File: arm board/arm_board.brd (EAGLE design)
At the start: 76.2 x 159.1 mm, 125 parts, among them J1 APPPP45_PCB_HORIZ_RIGHT, J17 APPPP45_PCB_HORIZ_RIGHT, J18 APPPP45_PCB_HORIZ_RIGHT, J19 ENCODER, J2 APPPP45_PCB_HORIZ_RIGHT, J20 ENCODER, J21 ENCODER, J22 ENCODER, J24 ENCODER, J3 APPPP45_PCB_HORIZ_RIGHT, J5 SERVOMOLEX_SL_VERT_TH, J6 SL02, Q1 Q_IRF7437SMD, U1 TIVA-1294

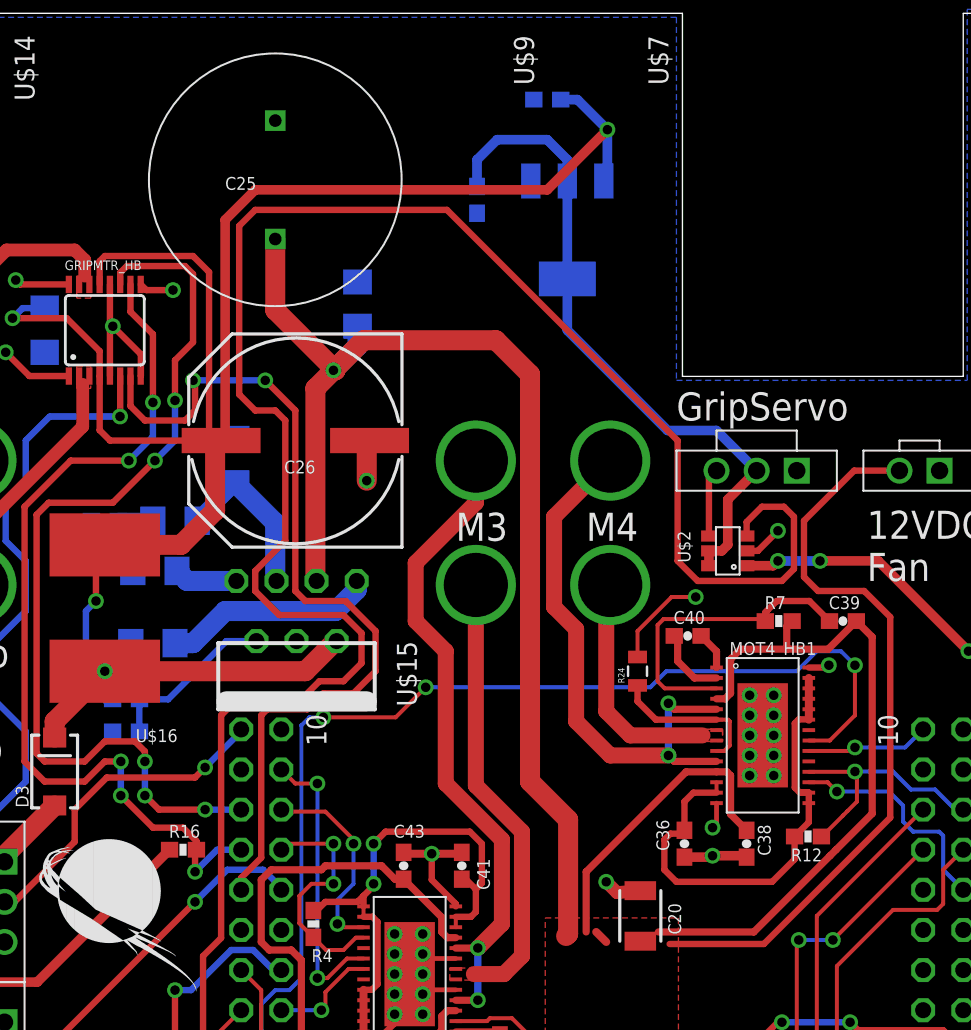
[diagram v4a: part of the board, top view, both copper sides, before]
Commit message: Swapped servo regulator input to draw from 12V line
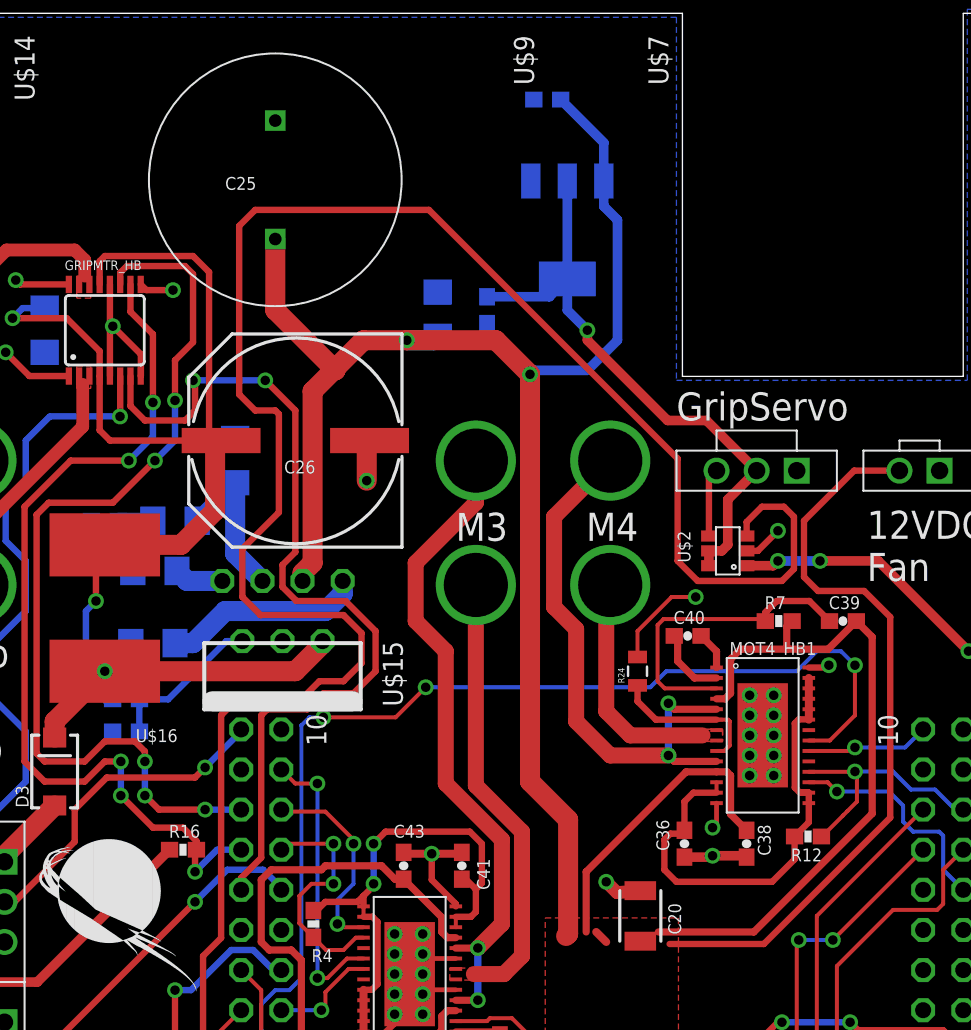
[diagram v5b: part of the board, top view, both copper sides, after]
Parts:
- moved C13 7.01 mm to (36.2, 140.3)
- moved C32 5.12 mm to (33.1, 140.1)
- moved U$15 0.89 mm to (23.2, 119.4)
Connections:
- net 12VMTR_PWR: now also C12.1, U$18.3
- net 7VMTR_PWR: no longer C12.1, U$18.3
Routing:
- net 7VMTR_PWR: track 114.7 -> 67.1 mm, vias 3 -> 2
- net 12VMTR_PWR: track 409.5 -> 431.8 mm, vias 5 -> 6
- net 5VSERVO_PWR: track 42.7 -> 38.0 mm, vias 0 -> 1
- net GRIPMTR_PHASE: track 55.9 -> 56.9 mm
- net N$9: track 4.02 -> 3.13 mm
- net N$10: track 11.0 -> 10.1 mm
- net N$33: track 25.5 -> 24.7 mm
- net N$15: track 13.5 -> 12.7 mm

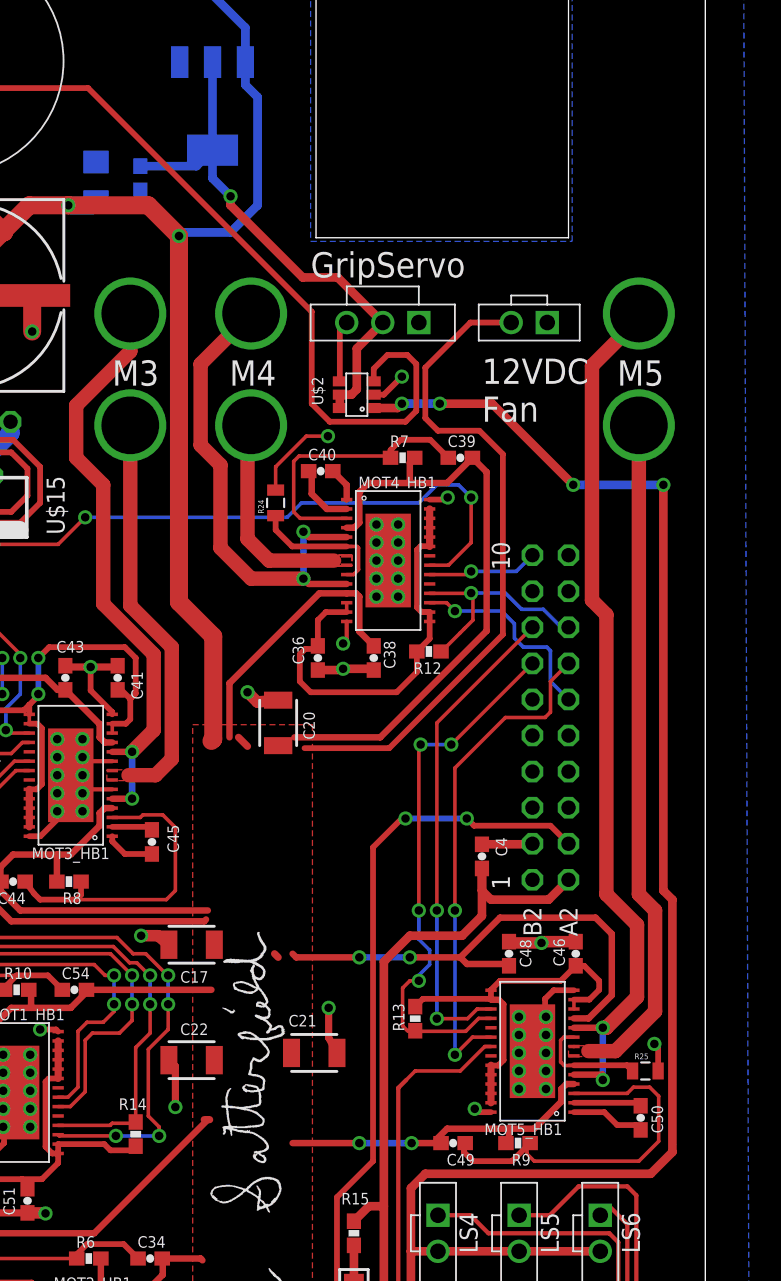
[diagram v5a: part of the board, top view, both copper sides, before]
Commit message: Changed sense resistor size
Miscalculated originally; it needs 2 watt rating
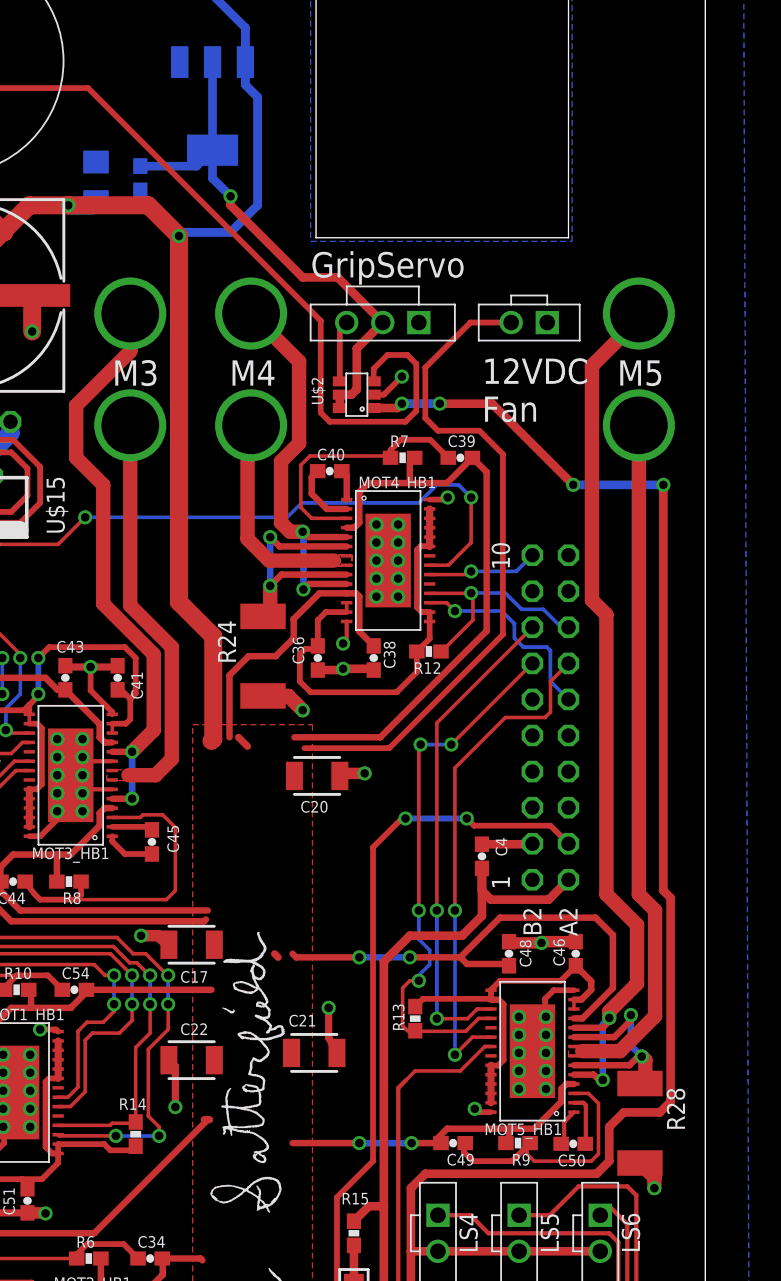
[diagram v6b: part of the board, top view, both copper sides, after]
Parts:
- removed R25: .22, SparkFun-Resistors:0805
- added R28: .22, SparkFun-Resistors:R2512
- R24: device SparkFun-Resistors:0805 -> SparkFun-Resistors:R2512
- moved R24 10.8 mm to (44.8, 106.7), turned to 270 degrees
- moved C50 5.09 mm to (66.7, 72.3), turned to 180 degrees
- moved C20 4.63 mm to (48.6, 98.2), turned to 180 degrees
- moved C40 0.63 mm to (49.5, 119.7)
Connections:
- net GND: now also R28.2; no longer R25.2
- net N$6: now also R28.1; no longer R25.1
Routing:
- net N$26: track 26.6 -> 18.0 mm
- net N$6: track 7.91 -> 16.1 mm, vias 0 -> 2
- net N$5: track 9.88 -> 17.2 mm, vias 0 -> 2
- net MOT4_1: track 35.0 -> 29.0 mm
- net GND: track 178.0 -> 174.5 mm
- net N$27: track 5.22 -> 2.60 mm
- net N$20: track 20.0 -> 18.7 mm
- net N$28: track 4.79 -> 3.64 mm
- net HB_3.3_OUTPUT8: track 27.5 -> 26.4 mm
- net 12VMTR_PWR: track 431.8 -> 432.7 mm
- net LOG_PWR_3.3V: track 405.4 -> 404.5 mm
- net MOT5_2: track 47.6 -> 48.2 mm
- net MOT5_1: track 62.3 -> 62.8 mm

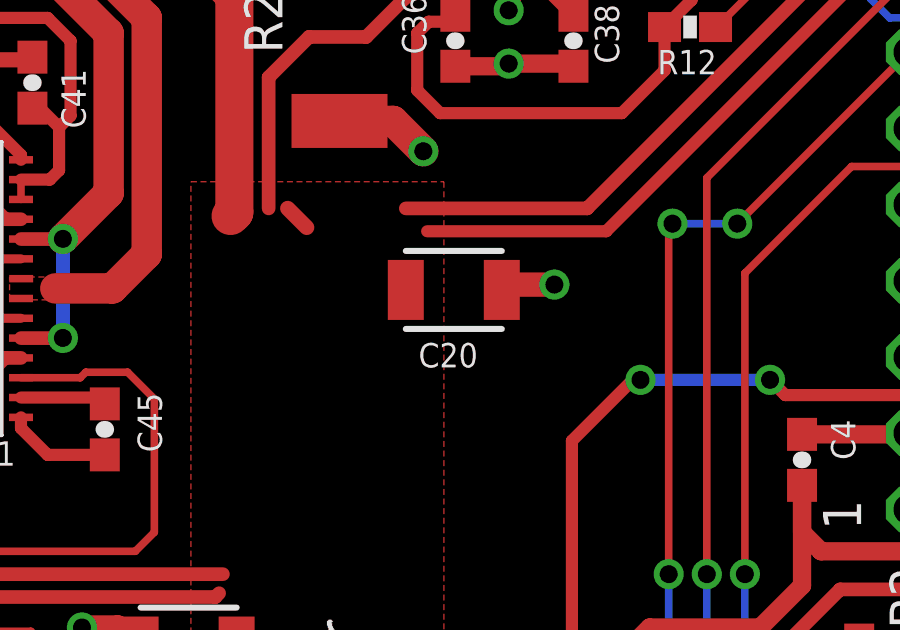
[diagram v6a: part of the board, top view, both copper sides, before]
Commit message: Spacing adjustment on one capacitor
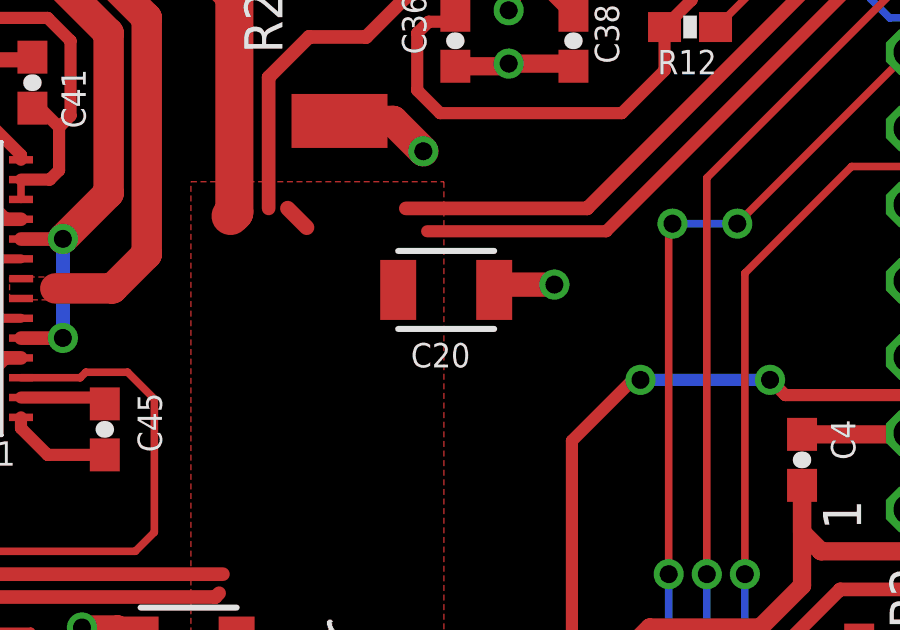
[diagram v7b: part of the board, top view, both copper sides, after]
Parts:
- moved C20 0.25 mm to (48.4, 98.2)
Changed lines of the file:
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@@
 <attribute name="VALUE" x="38.9018" y="85.66" size="0.4064" layer="27"/>
 </element>
-<element name="C20" library="SparkFun-Capacitors" package="1210" value="100uF" x="48.641" y="98.2472" smashed="yes" rot="R180">
-<attribute name="NAME" x="49.441" y="96.4772" size="0.8128" layer="25" rot="R180"/>
-<attribute name="VALUE" x="49.541" y="98.9472" size="0.4064" layer="27" rot="R180"/>
+<element name="C20" library="SparkFun-Capacitors" package="1210" value="100uF" x="48.387" y="98.2472" smashed="yes" rot="R180">
+<attribute name="NAME" x="49.187" y="96.4772" size="0.8128" layer="25" rot="R180"/>
+<attribute name="VALUE" x="49.287" y="98.9472" size="0.4064" layer="27" rot="R180"/>
 </element>
 <element name="C21" library="SparkFun-Capacitors" package="1210" value="100uF" x="48.4378" y="78.74" smashed="yes" rot="R180">
@@
 <contactref element="R24" pad="2"/>
 <wire x1="51.9938" y1="98.425" x2="50.4188" y2="98.425" width="0.8128" layer="1"/>
-<wire x1="50.4188" y1="98.425" x2="50.241" y2="98.2472" width="0.8128" layer="1"/>
+<wire x1="50.4188" y1="98.425" x2="49.987" y2="98.2472" width="0.8128" layer="1"/>
 <wire x1="44.831" y1="103.88" x2="46.615" y2="103.88" width="1.016" layer="1"/>
 <wire x1="46.615" y1="103.88" x2="47.625" y2="102.87" width="1.016" layer="1"/>

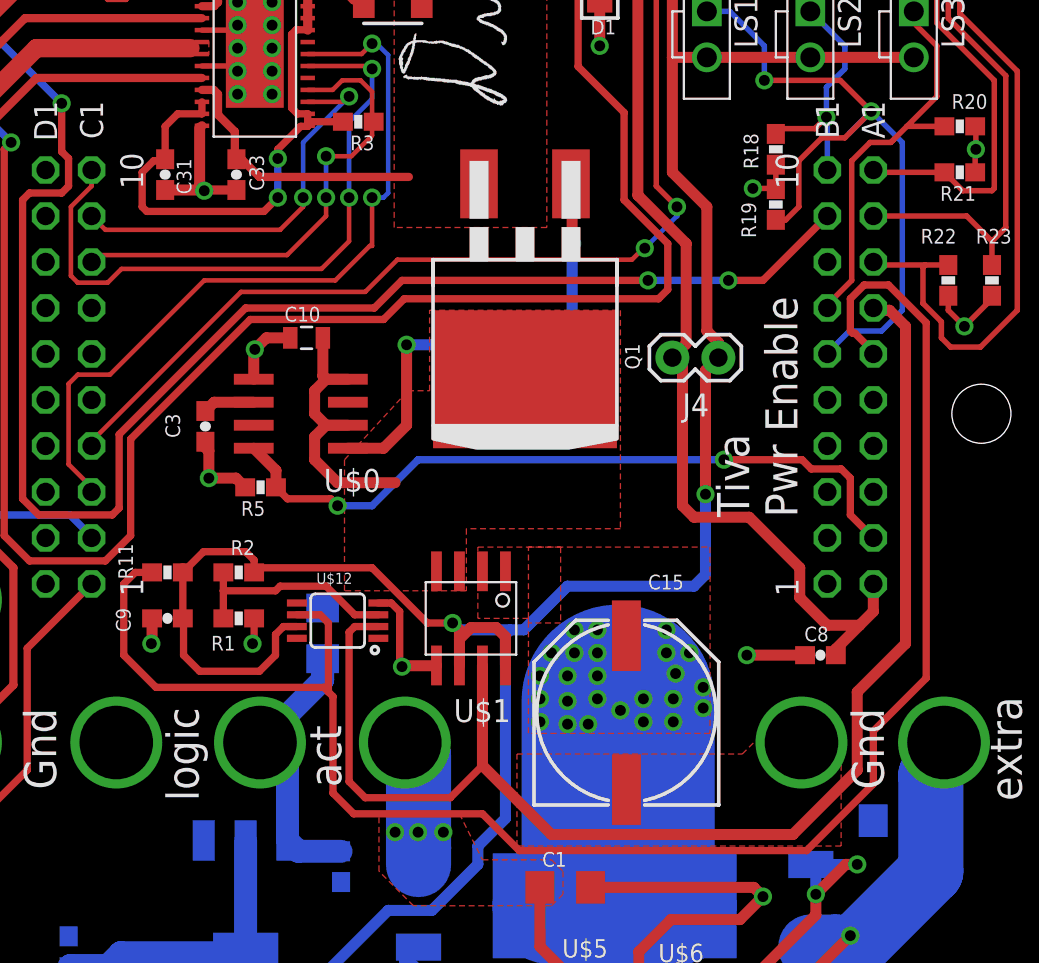
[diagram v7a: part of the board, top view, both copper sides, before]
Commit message: Removed opamp and components
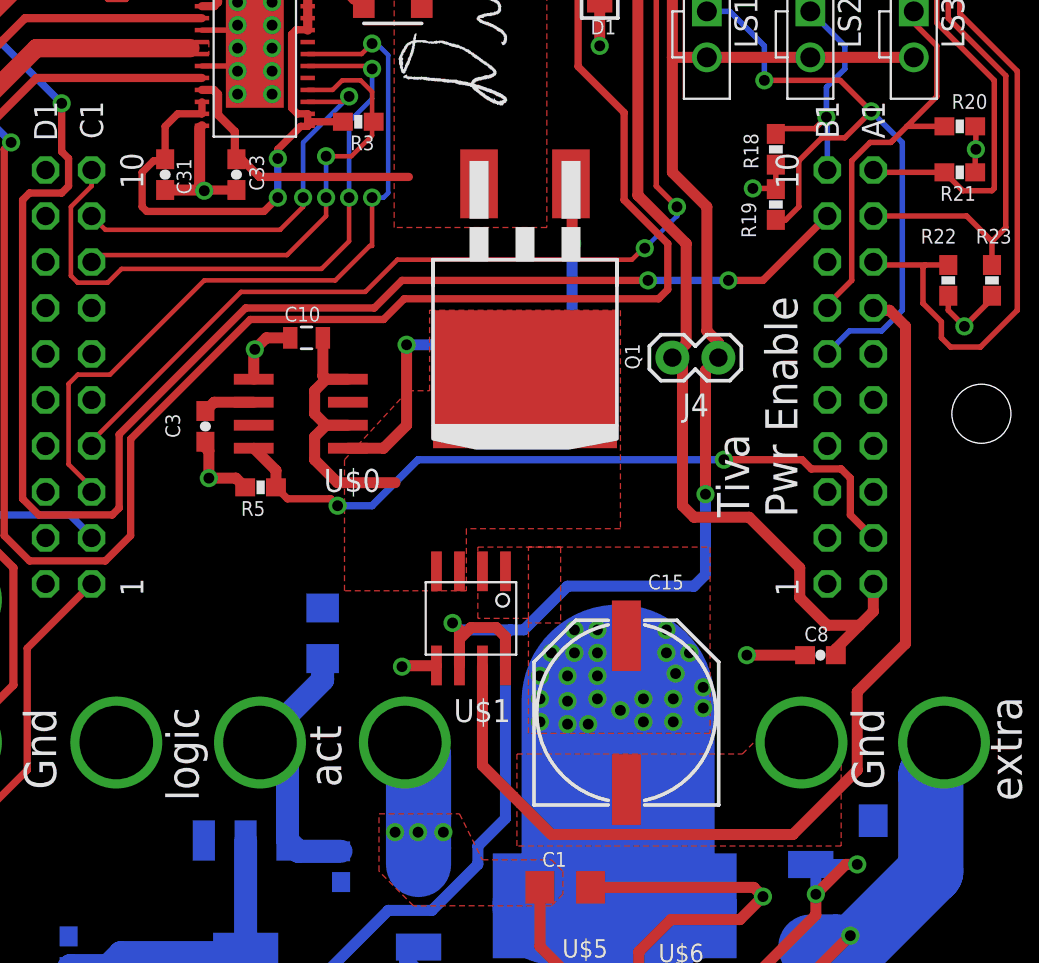
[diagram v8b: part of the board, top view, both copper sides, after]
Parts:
- removed C9: 2.2uF, SparkFun-Capacitors:0603-CAP
- removed R1: 1.2k, SparkFun-Passives:0603-RES
- removed R11: 10k, SparkFun-Passives:0603-RES
- removed R2: 1k, SparkFun-Passives:0603-RES
- removed U$12: OPA140, MRDT-Semiconductors:MSOP8
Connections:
- removed net AMP_RD: U$1.7, U$12.2, U1.PD3
- removed net N$7: R1.1, R2.2, U$12.3
- new net CURRENT_INPUT: U$1.7, U1.PD3
- net GND: no longer C9.2, R1.2, U$12.4
- net LOG_PWR_3.3V: no longer C9.1, R11.2, R2.1, U$12.7
- net MAIN_PWR_SWITCH_NFAULT: no longer R11.1, U$12.6
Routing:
- net MAIN_PWR_SWITCH_NFAULT: track 97.7 -> 0.00 mm
- net AMP_RD: track 75.6 -> 0.00 mm
- net CURRENT_INPUT: track 0.00 -> 57.1 mm
- net LOG_PWR_3.3V: track 404.5 -> 373.8 mm
- net N$7: track 11.9 -> 0.00 mm
- net GND: track 174.8 -> 167.6 mm, vias 83 -> 81
- net LS1_SIG: track 40.3 -> 38.6 mm
